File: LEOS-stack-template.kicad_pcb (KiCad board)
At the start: 2 copper layers, 100 x 100 mm, 22 parts, among them J1 MicroFit_1x4, J2 MicroFit_1x4, U1 MCP2562FD, U2 MCP2518FD, Y1 40 MHz

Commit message: Add design rule overrides and auto board naming
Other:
- board text added: "${ISSUE_DATE}"
- board text added: "Be sure to update the information block at the bottom of the page!"
- board text added: "LEOS ${TITLE} Rev ${REVISION}"
- board text removed: "LEOS CHANGE THIS NAME Rev. 3"

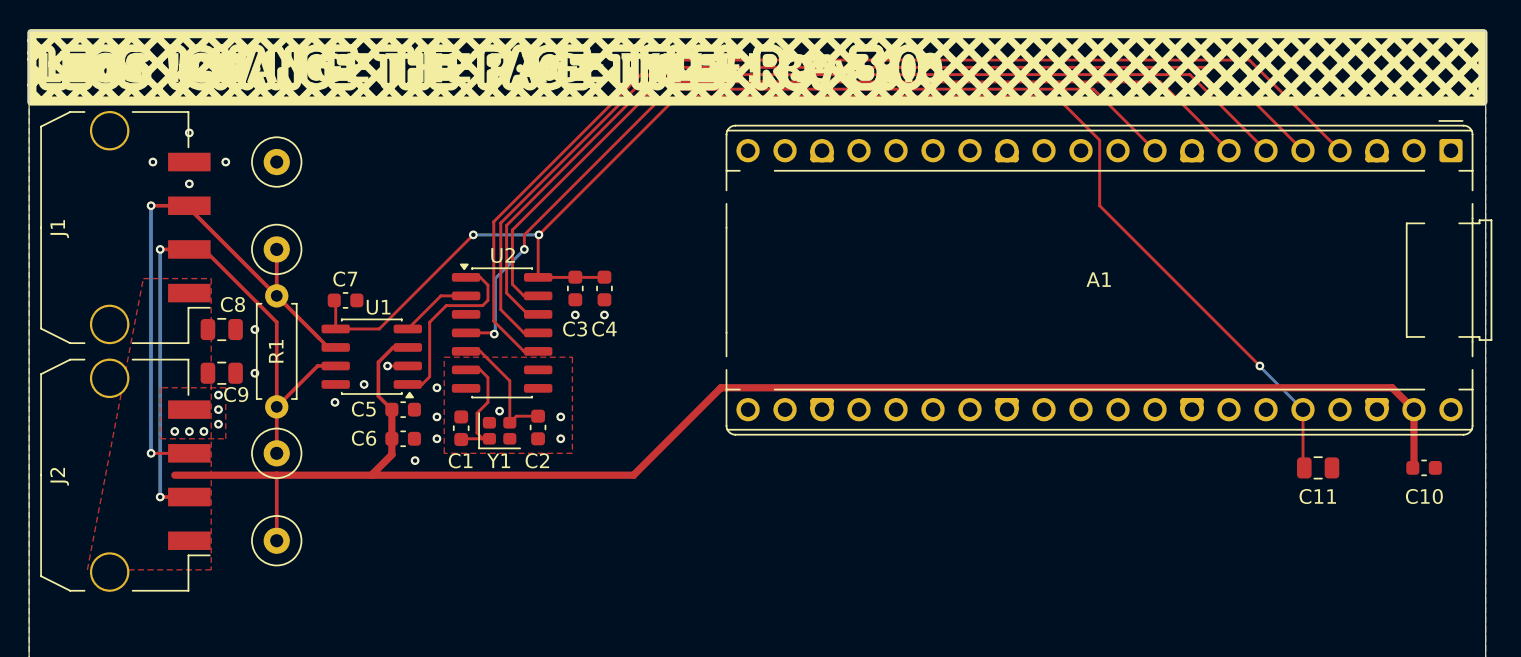
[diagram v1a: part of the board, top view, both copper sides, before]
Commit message: Version 3.0
This revision includes a number of changes, notably:
- larger 0805/1206 parts and reduced BOM
- SMD/TH Pads for the Pico Devboard
- Document variable Silkscreen text
- Text documentation throughout schematics
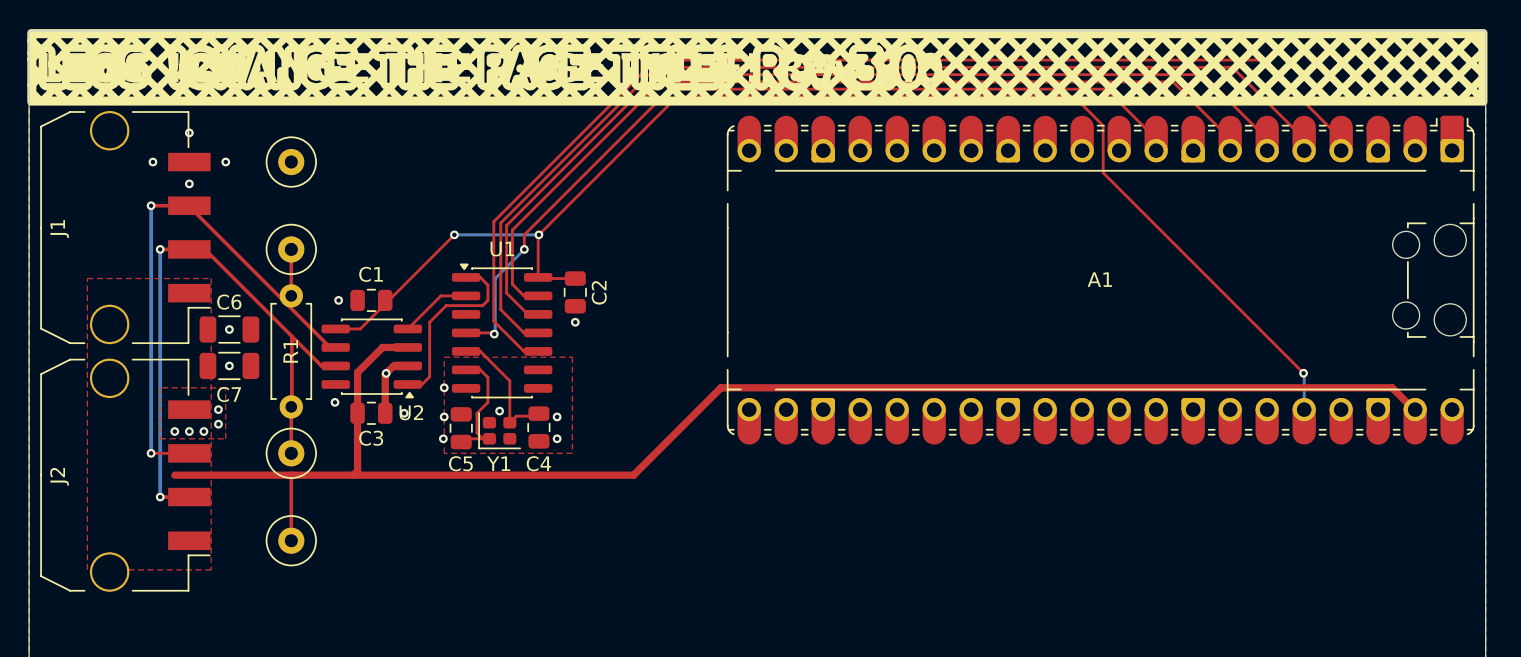
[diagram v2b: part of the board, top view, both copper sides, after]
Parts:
- removed C10: 0.1u, Capacitor_SMD:C_0603_1608Metric
- removed C11: 10u, Capacitor_SMD:C_0805_2012Metric
- removed the C4 at (139.5, 67.7)
- removed the C5 at (125.7, 76.0)
- removed the C6 at (125.7, 78.0)
- removed the C7 at (121.7, 68.5)
- added C1: 0.1u, Capacitor_SMD:C_0805_2012Metric, F.Cu at (123.5, 68.5)
- added C2: 0.1u, Capacitor_SMD:C_0805_2012Metric, F.Cu at (137.5, 68.0)
- A1: footprint Module:RaspberryPi_Pico_Common_THT -> Module:RaspberryPi_Pico_Common_Unspecified
- C3: footprint Capacitor_SMD:C_0603_1608Metric -> Capacitor_SMD:C_0805_2012Metric
- C4: renamed from C2; footprint Capacitor_SMD:C_0603_1608Metric -> Capacitor_SMD:C_0805_2012Metric
- C5: renamed from C1; footprint Capacitor_SMD:C_0603_1608Metric -> Capacitor_SMD:C_0805_2012Metric
- C6: renamed from C8; footprint Capacitor_SMD:C_0805_2012Metric -> Capacitor_SMD:C_1206_3216Metric
- C7: renamed from C9; footprint Capacitor_SMD:C_0805_2012Metric -> Capacitor_SMD:C_1206_3216Metric
- moved A1 25.6 mm to (173.6, 67.1)
- moved C3 16.4 mm to (123.5, 76.2), turned to 0 degrees
- moved R1 1.00 mm to (118.0, 68.2)
- moved TP1 1.00 mm to (118.0, 79.0)
- moved TP2 1.00 mm to (118.0, 65.0)
- moved TP3 1.00 mm to (118.0, 85.0)
- moved TP4 1.00 mm to (118.0, 59.0)
- moved C7 0.73 mm to (113.8, 73.0)
- moved C6 0.53 mm to (113.8, 70.5)
- moved C4 0.06 mm to (135.0, 77.2)
- renumbered U2 to U1, U1 to U2
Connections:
- net Net-(U1-RXD) renamed /CANbus/RXCAN
- net Net-(U1-TXD) renamed /CANbus/TXCAN
- C3 pad 1: VDD -> +5V
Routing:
- net /CANbus/CAN-: track 51.3 -> 39.1 mm
- net VDD: track 97.8 -> 90.8 mm
- net +5V: track 107.8 -> 104.0 mm
- net GND: track 1.39 -> 4.46 mm, vias 24 -> 22
- net /CANbus/CAN+: track 42.3 -> 41.3 mm
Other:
- board text added: "Be sure to update the information block at the bottom of the page! (Then delete me)"
- board text added: "Populate R1 with 120Ω if board is at end of bus."
- board text removed: "Be sure to update the information block at the bottom of the page!"
